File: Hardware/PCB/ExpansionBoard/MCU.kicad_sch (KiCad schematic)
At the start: 0 parts

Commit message: INT BUS
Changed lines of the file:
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@@
 	(label "SCLK"
 		(at 74.93 62.23 0)
+		(fields_autoplaced yes)
 		(effects
 			(font
@@
 		)
 	)
+	(hierarchical_label "INT"
+		(shape input)
+		(at 48.26 72.39 180)
+		(fields_autoplaced yes)
+		(effects
+			(font
+				(size 1.27 1.27)
+			)
+			(justify right)
+		)
+	)

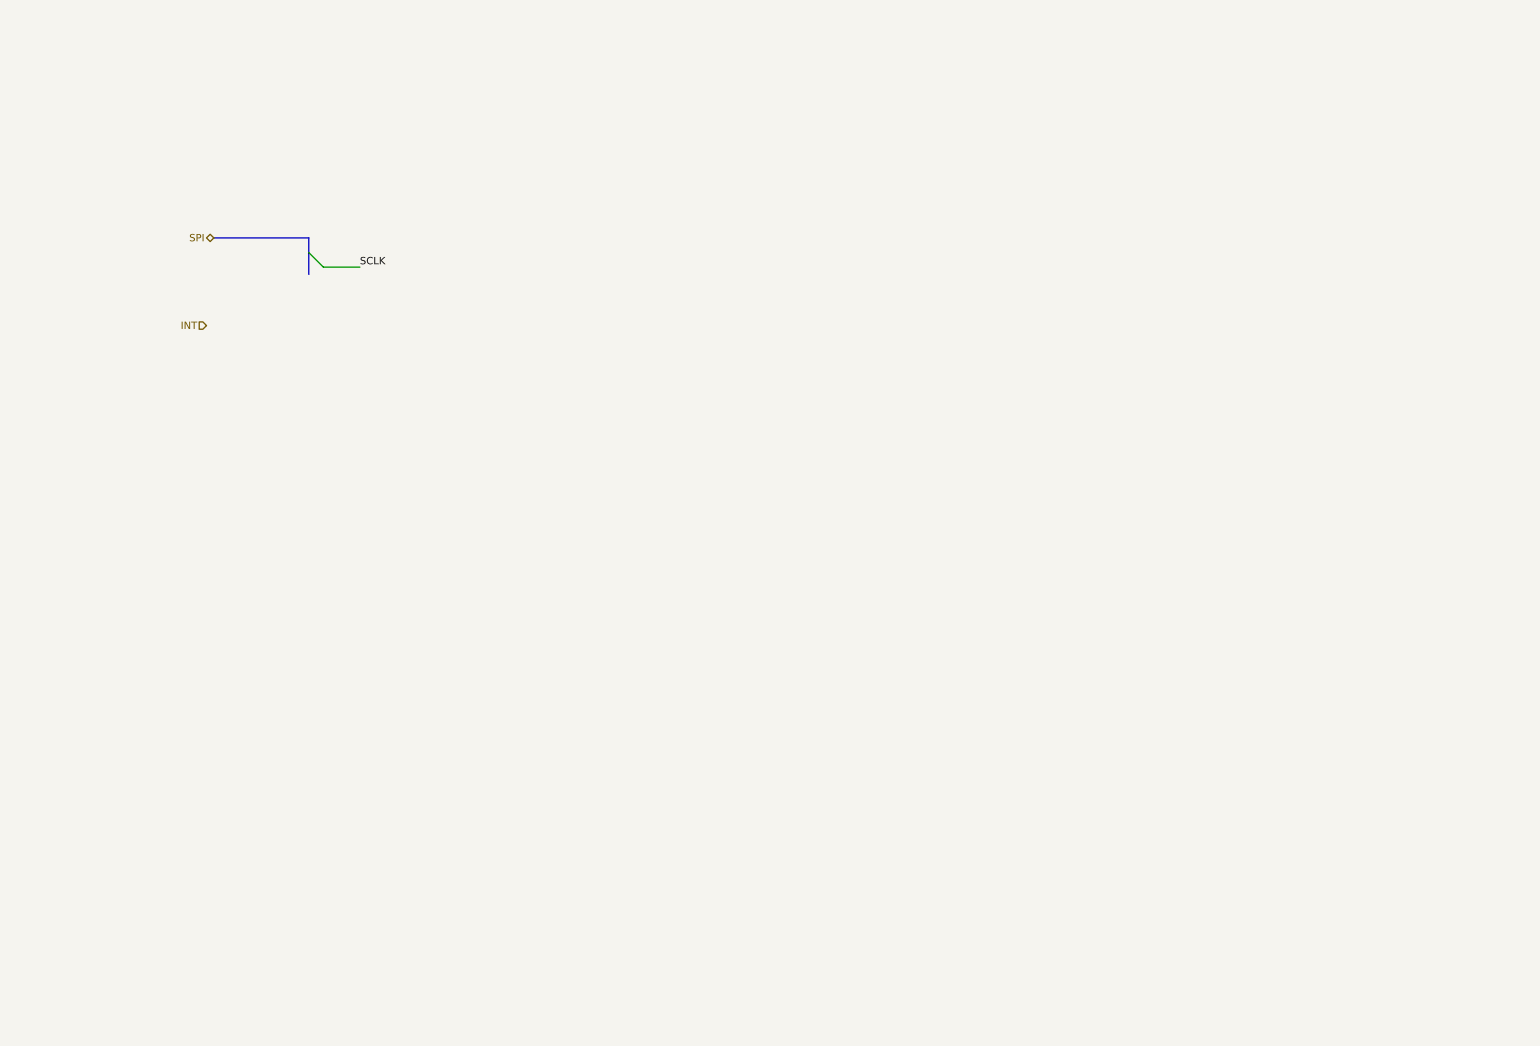
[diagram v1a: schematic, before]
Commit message: added PINOUT to mcu and UART USB CHIP
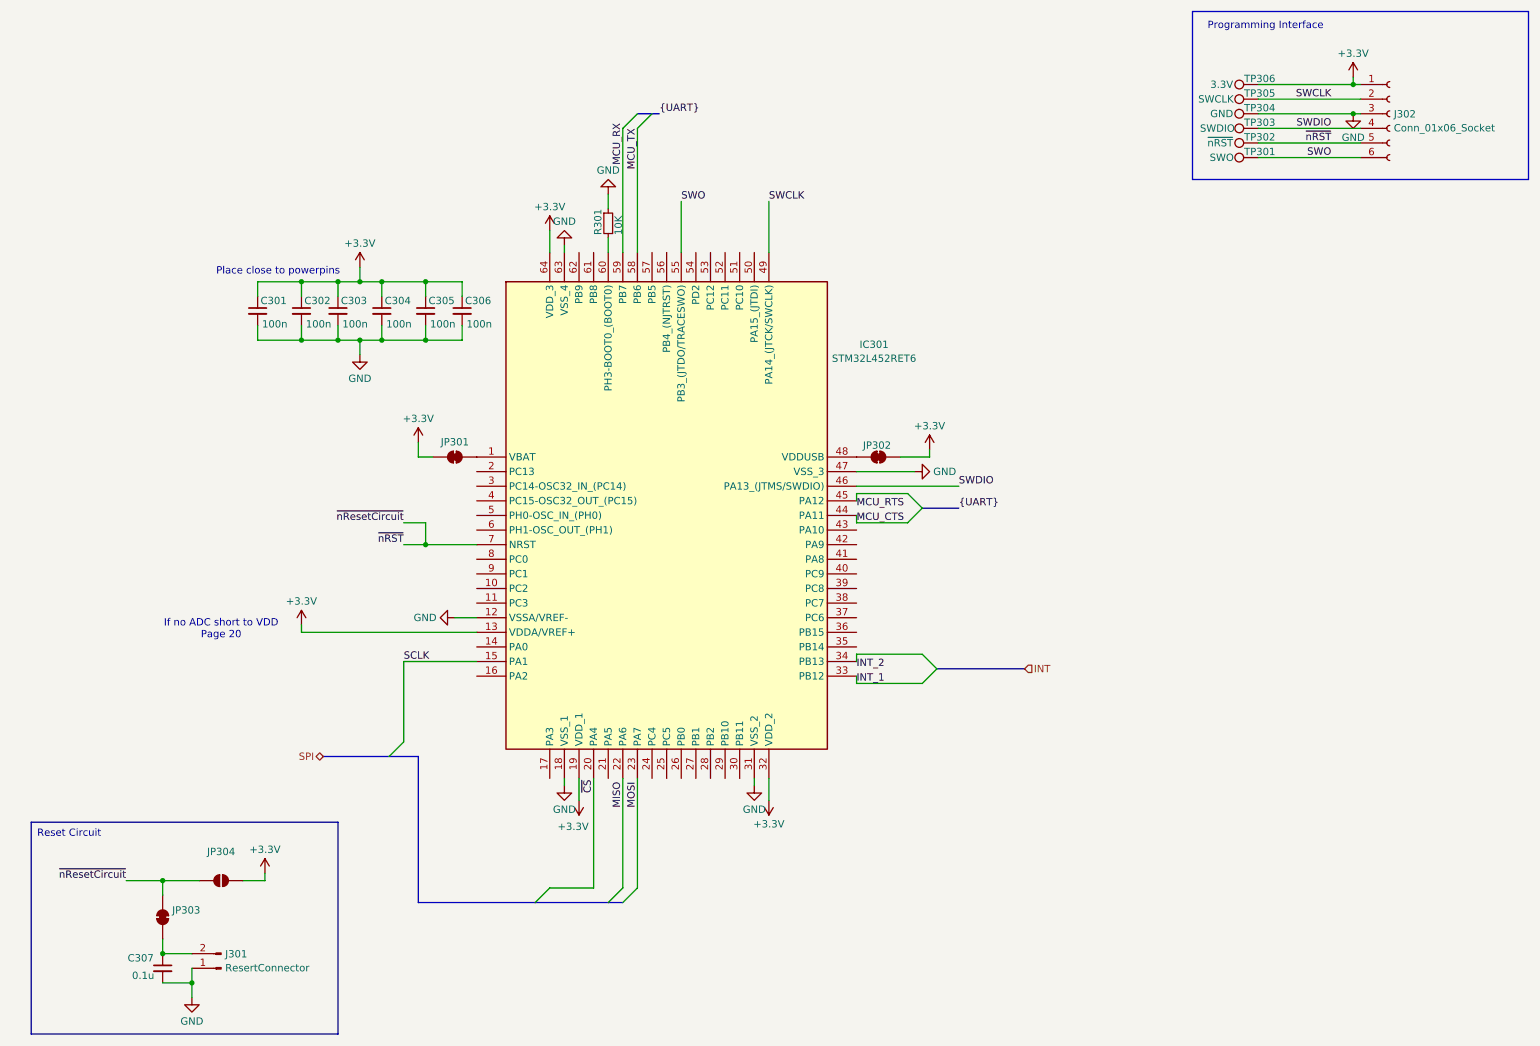
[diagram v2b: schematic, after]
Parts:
- added C301, C302, C303, C304, C305, C306: 100n, symbol Device:C_Small
- added C307: 0.1u, symbol Device:C_Small
- added IC301: STM32L452RET6, QFP50P1200X1200X160-64N, symbol SamacSys_Parts:STM32L452RET6
- added J301: ResertConnector, symbol Connector:Conn_01x02_Pin
- added J302: Conn_01x06_Socket, Connector:Tag-Connect_TC2030-IDC-FP_2x03_P1.27mm_Vertical, symbol Connector:Conn_01x06_Socket
- added JP301, JP302, JP303: SolderJumper_2_Bridged, symbol Jumper:SolderJumper_2_Bridged
- added JP304: SolderJumper_2_Open, symbol Jumper:SolderJumper_2_Open
- added R301: 10K, symbol Device:R_Small
- added TP301: SWO, symbol Connector:TestPoint
- added TP302: ~{nRST}, symbol Connector:TestPoint
- added TP303: SWDIO, symbol Connector:TestPoint
- added TP304: GND, symbol Connector:TestPoint
- added TP305: SWCLK, symbol Connector:TestPoint
- added TP306: 3.3V, symbol Connector:TestPoint
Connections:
- net SCLK: now also IC301.15 (PA1)
- new net: C307.1, J301.2 (Pin_2), JP303.1 (A)
- new net: IC301.60 (PH3-BOOT0_(BOOT0)), R301.2
- new net: IC301.1 (VBAT), JP301.2 (B)
- new net: IC301.48 (VDDUSB), JP302.2 (B)
- new net +3.3V: C301.1, C302.1, C303.1, C304.1, C305.1, C306.1, IC301.13 (VDDA/VREF+), IC301.19 (VDD_1), IC301.32 (VDD_2), IC301.64 (VDD_3), J302.1 (Pin_1), JP301.1 (A), JP302.1 (A), JP304.2 (B), TP306.1
- new net GND: C301.2, C302.2, C303.2, C304.2, C305.2, C306.2, C307.2, IC301.12 (VSSA/VREF-), IC301.18 (VSS_1), IC301.31 (VSS_2), IC301.47 (VSS_3), IC301.63 (VSS_4), J301.1 (Pin_1), J302.3 (Pin_3), R301.1, TP304.1
- new net INT_1: IC301.33 (PB12)
- new net MCU_CTS: IC301.44 (PA11)
- new net MCU_RX: IC301.59 (PB7)
- new net MCU_TX: IC301.58 (PB6)
- new net MISO: IC301.22 (PA6)
- new net MOSI: IC301.23 (PA7)
- new net SWCLK: IC301.49 (PA14_(JTCK/SWCLK)), J302.2 (Pin_2), TP305.1
- new net SWDIO: IC301.46 (PA13_(JTMS/SWDIO)), J302.4 (Pin_4), TP303.1
- new net SWO: IC301.55 (PB3_(JTDO/TRACESWO)), J302.6 (Pin_6), TP301.1
- new net ~{CS}: IC301.20 (PA4)
- new net ~{nRST}: IC301.7 (NRST), J302.5 (Pin_5), JP303.2 (B), JP304.1 (A), TP302.1
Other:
- note added: "If no ADC short to VDD Page 20"
- note added: "Place close to powerpins"
- note added: "Programming Interface"
- note added: "Reset Circuit"

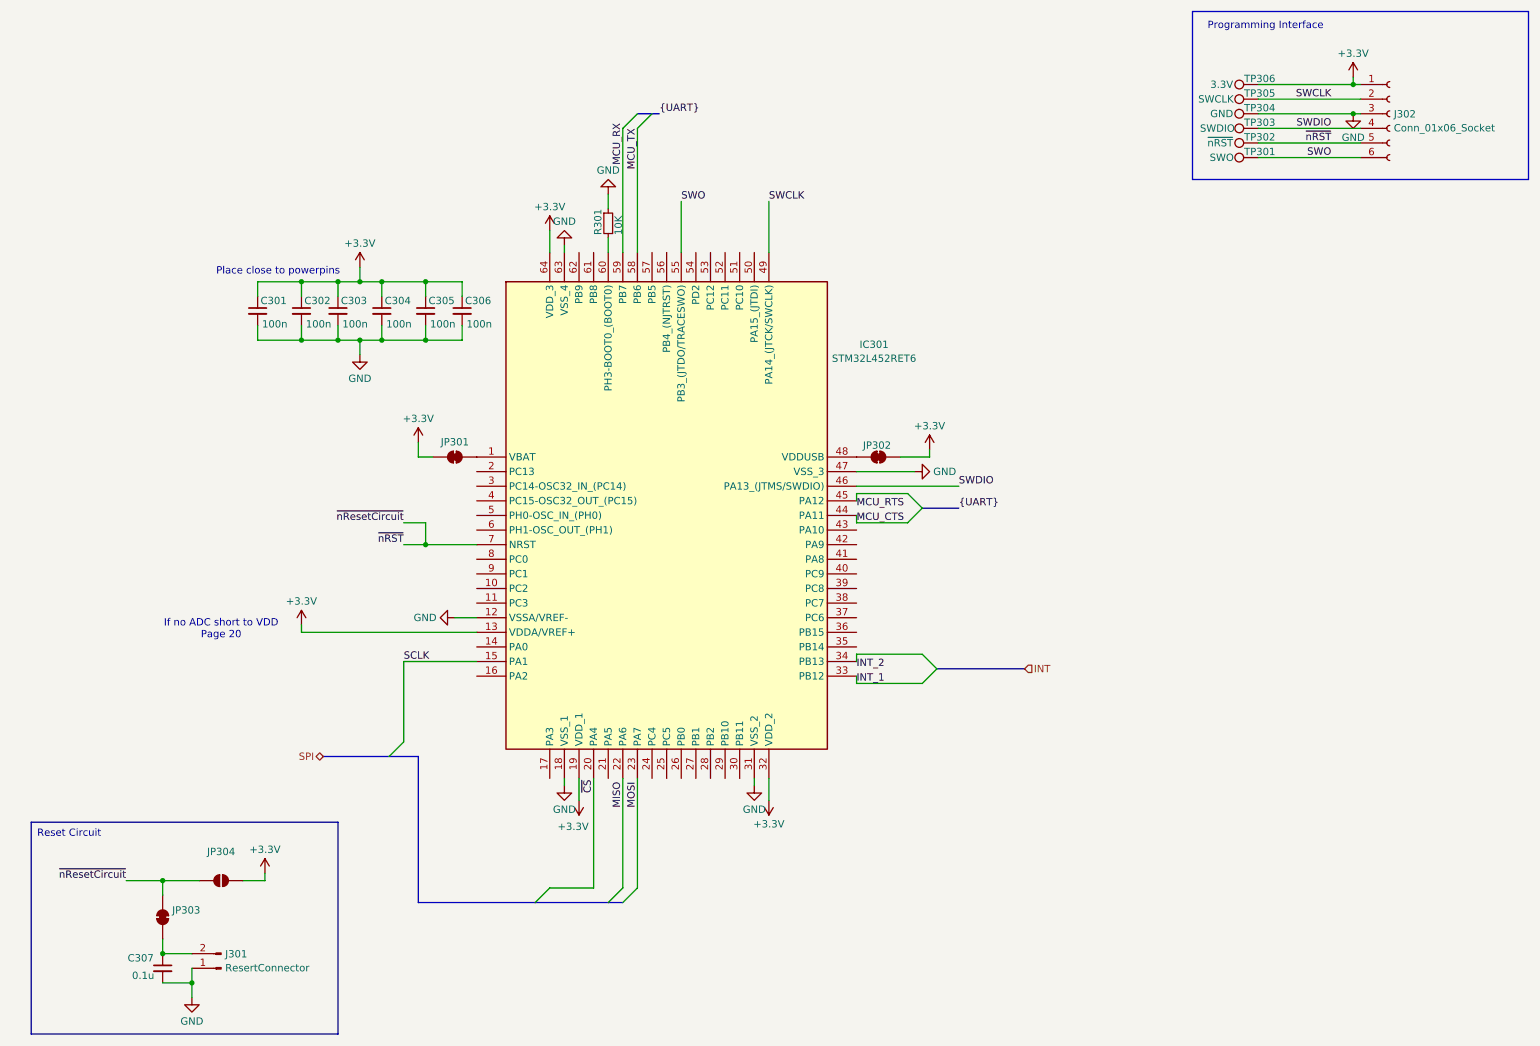
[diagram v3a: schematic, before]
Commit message: DONE: PWR LED MISSING AND AIRSPEED
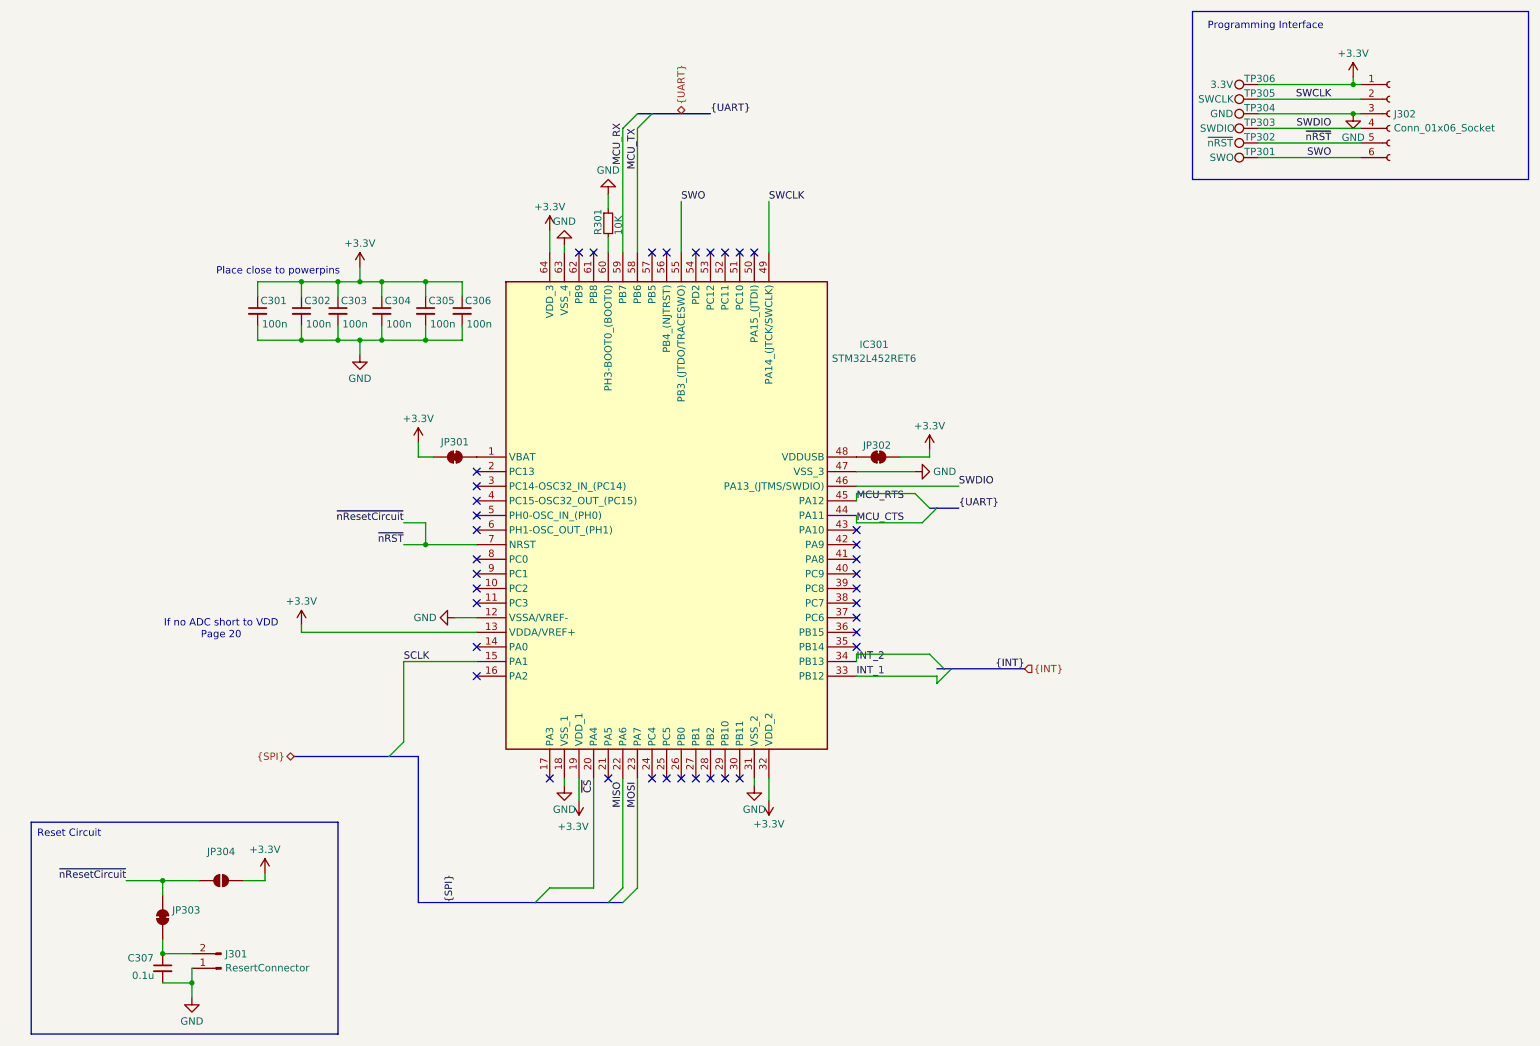
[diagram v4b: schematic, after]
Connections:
- net INT_2: now also IC301.34 (PB13)
- net MCU_RTS: now also IC301.45 (PA12)
- no-connect marks 0 -> 38

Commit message: finished schema
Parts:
- C301, C302, C303, C304, C305, C306, C307: footprint (none) -> Capacitor_SMD:C_0805_2012Metric_Pad1.18x1.45mm_HandSolder
- J301: footprint (none) -> Connector_PinHeader_2.54mm:PinHeader_1x02_P2.54mm_Vertical
- JP301, JP302, JP303: footprint (none) -> Jumper:SolderJumper-2_P1.3mm_Bridged_RoundedPad1.0x1.5mm
- JP304: footprint (none) -> Jumper:SolderJumper-2_P1.3mm_Open_RoundedPad1.0x1.5mm
- R301: footprint (none) -> Resistor_SMD:R_0805_2012Metric_Pad1.20x1.40mm_HandSolder
- TP301, TP302, TP303, TP304, TP305, TP306: footprint (none) -> TestPoint:TestPoint_Pad_D3.0mm
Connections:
- net INT: now reaches IC301.41 (PA8)
- net SCL: now reaches IC301.42 (PA9)
- net SDA: now reaches IC301.43 (PA10)
- no-connect marks 38 -> 35

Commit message: to pcb
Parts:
- IC301: footprint QFP50P1200X1200X160-64N -> SamacSys_Parts:QFP50P1200X1200X160-64N
- TP301, TP302, TP303, TP304, TP305, TP306: footprint TestPoint:TestPoint_Pad_D3.0mm -> TestPoint:TestPoint_Pad_D1.5mm
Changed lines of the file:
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@@
 			)
 		)
-		(property "Footprint" "TestPoint:TestPoint_Pad_D3.0mm"
+		(property "Footprint" "TestPoint:TestPoint_Pad_D1.5mm"
 			(at 231.14 35.56 0)
 			(effects
@@
 			)
 		)
-		(property "Footprint" "TestPoint:TestPoint_Pad_D3.0mm"
+		(property "Footprint" "TestPoint:TestPoint_Pad_D1.5mm"
 			(at 231.14 38.1 0)
 			(effects
@@
 			)
 		)
-		(property "Footprint" "QFP50P1200X1200X160-64N"
+		(property "Footprint" "SamacSys_Parts:QFP50P1200X1200X160-64N"
 			(at 157.48 162.23 0)
 			(effects
@@
 			)
 		)
-		(property "Footprint" "TestPoint:TestPoint_Pad_D3.0mm"
+		(property "Footprint" "TestPoint:TestPoint_Pad_D1.5mm"
 			(at 231.14 30.48 0)
 			(effects
@@
 			)
 		)
-		(property "Footprint" "TestPoint:TestPoint_Pad_D3.0mm"
+		(property "Footprint" "TestPoint:TestPoint_Pad_D1.5mm"
 			(at 231.14 25.4 0)
 			(effects
@@
 			)
 		)
-		(property "Footprint" "TestPoint:TestPoint_Pad_D3.0mm"
+		(property "Footprint" "TestPoint:TestPoint_Pad_D1.5mm"
 			(at 231.14 27.94 0)
 			(effects
@@
 			)
 		)
-		(property "Footprint" "TestPoint:TestPoint_Pad_D3.0mm"
+		(property "Footprint" "TestPoint:TestPoint_Pad_D1.5mm"
 			(at 231.14 33.02 0)
 			(effects

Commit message: added Cube Project, SD Card and Tillt Switch
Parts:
- added C308: 1400n, Capacitor_SMD:C_0805_2012Metric_Pad1.18x1.45mm_HandSolder, symbol Device:C_Small
- added J303: MEM2061-01-188-00-A, SamacSys_Parts:MEM20610118800A, symbol SamacSys_Parts:MEM2061-01-188-00-A
- added R302, R303: 0, Resistor_SMD:R_0805_2012Metric_Pad1.20x1.40mm_HandSolder, symbol Device:R_Small
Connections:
- net +3.3V: now also C308.1, J303.P4 (VDD)
- net GND: now also C308.2, J303.G1 (GND_1), J303.G2 (GND_2), J303.P6 (VSS)
- net MISO: now also IC301.10 (PC2), J303.P7 (DAT0)
- net MOSI: now also IC301.11 (PC3), J303.P3 (CMD)
- net CLK: now reaches IC301.29 (PB10)
- net CLK: now also J303.P5 (CLK)
- net Angle_Indicator_1: now reaches IC301.5 (PH0-OSC_IN_(PH0))
- net Angle_Indicator_2: now reaches IC301.6 (PH1-OSC_OUT_(PH1))
- net CardDetect: now reaches IC301.61 (PB8)
- net CardDetect: now also R302.2, R303.2
- net NSS: now reaches IC301.62 (PB9)
- net NSS: now also J303.P2 (CD/DAT3)
- new net: J303.CD2 (CARD_DETECT_2), R302.1
- new net: J303.CD1 (CARD_DETECT_1), R303.1
- no-connect marks 35 -> 30
